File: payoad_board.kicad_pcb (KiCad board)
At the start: 2 copper layers, 48.8 x 58 mm, 3 parts, among them J1 NMHH-1_bus, U3 RP2040 MCU board, U4 RP2040 MCU board

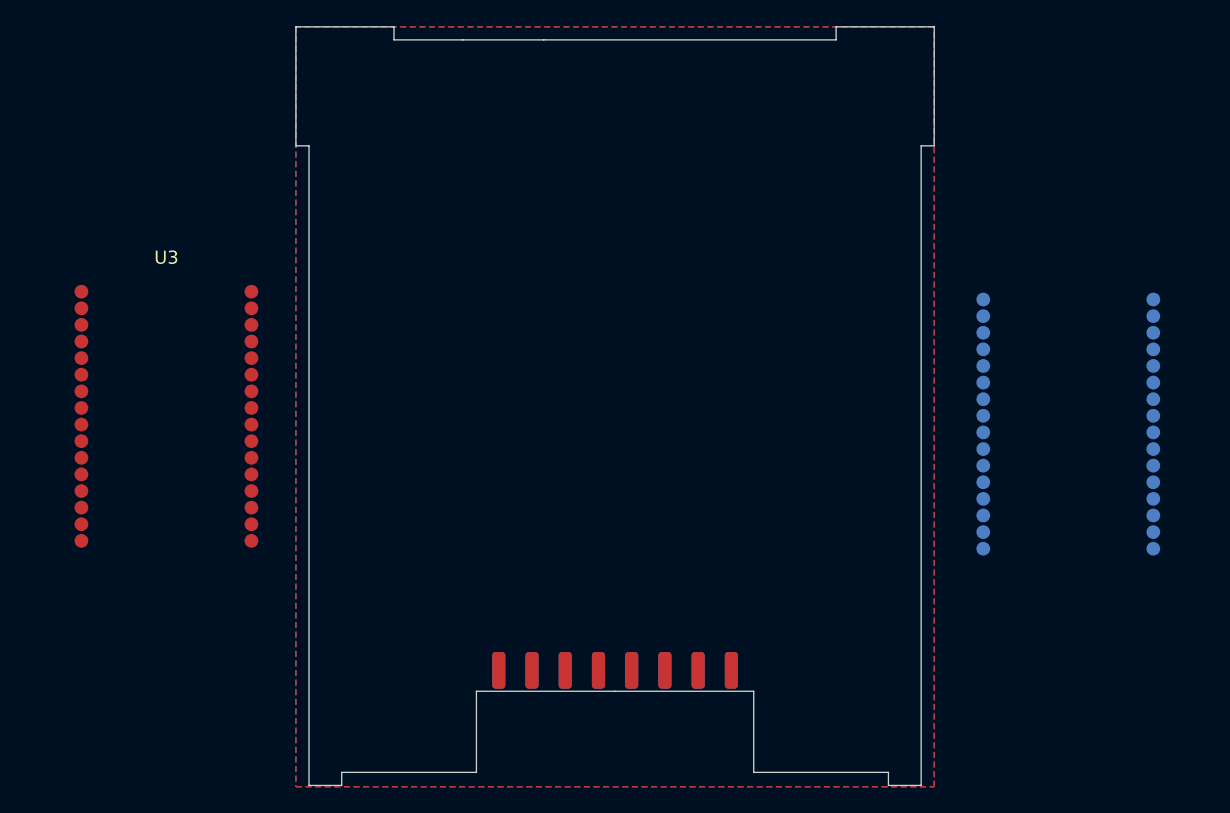
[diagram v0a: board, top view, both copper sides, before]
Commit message: Project libraries, PQ_bus connector symbol, CAN2 on the bus
- Add project-local symbol (pq.kicad_sym) and footprint library tables,
  both relative to ${KIPRJMOD}, so the project opens without extra setup
- New PQ_bus symbol: supply pins are power outputs, so ERC passes
  without PWR_FLAGs; replaces the generic 2x8 connector
- Bus connector footprint renamed to PQ_bus, 3D model assigned
- CAN2 routed to bus pins 6/8 (U2); CAN1 on pins 9/11 (U1)
- 1-Wire notes on the schematic, MCUs re-annotated to U1/U2
- README: PQ_bus pinout with DNC pins, library and file list

Co-Authored-By: Claude Opus 5.5 <noreply@anthropic.com>
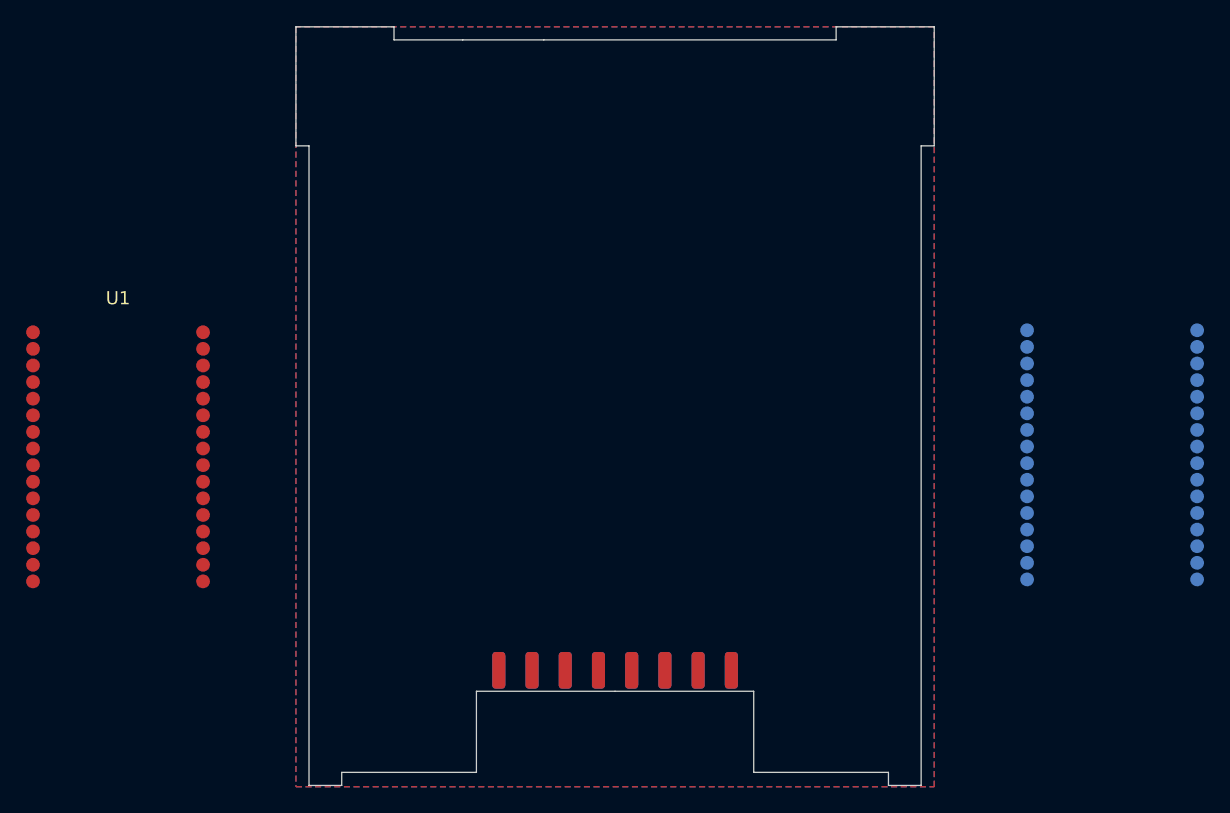
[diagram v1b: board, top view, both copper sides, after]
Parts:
- removed U3, U4: RP2040 MCU board, pq:MCU_board_127
- added U1: RP2040 MCU board, pq:MCU_board_127, F.Cu at (-38.0, -24.2)
- added U2: RP2040 MCU board, pq:MCU_board_127, B.Cu at (38.0, -24.2)
- J1: value NMHH-1_bus -> PQ_bus
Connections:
- J1 pad 6: CAN1_H -> CAN2_H
- J1 pad 8: CAN1_L -> CAN2_L

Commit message: Rename 1W/1-Wire signals to HDUART
1-Wire is a trademarked name, so the bus signals and MCU pin labels
are now called HDUART (HDUART_1, HDUART_2, GPIO05/HDUART1, ...).

Co-Authored-By: Claude Opus 5.5 <noreply@anthropic.com>
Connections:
- net 1W_1 renamed HDUART_1
- net 1W_2 renamed HDUART_2
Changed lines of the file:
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@@
 			(layers "B.Cu" "B.Mask" "B.Paste")
 			(roundrect_rratio 0.25)
-			(net "1W_2")
-			(pinfunction "1W_2_4")
+			(net "HDUART_2")
+			(pinfunction "HDUART_2_4")
 			(pintype "bidirectional")
 			(thermal_bridge_angle 45)
@@
 			(layers "F.Cu" "F.Mask" "F.Paste")
 			(roundrect_rratio 0.25)
-			(net "1W_1")
-			(pinfunction "1W_1_13")
+			(net "HDUART_1")
+			(pinfunction "HDUART_1_13")
 			(pintype "bidirectional")
 			(thermal_bridge_angle 45)
@@
 			)
 		)
-		(fp_text user "GPIO00_(1W2TX)"
+		(fp_text user "GPIO00_(HDUART2TX)"
 			(at -5.975 -8.18 0)
 			(unlocked yes)
@@
 			)
 		)
-		(fp_text user "GPIO01/1W2"
+		(fp_text user "GPIO01/HDUART2"
 			(at -5.975 -6.91 0)
 			(unlocked yes)
@@
 			)
 		)
-		(fp_text user "GPIO04_(1W1TX)"
+		(fp_text user "GPIO04_(HDUART1TX)"
 			(at -5.975 -3.1 0)
 			(unlocked yes)
@@
 			)
 		)
-		(fp_text user "GPIO05/1W1"
+		(fp_text user "GPIO05/HDUART1"
 			(at -5.975 -1.83 0)
 			(unlocked yes)
@@
 			(size 1.05 1.05)
 			(layers "F.Cu" "F.Mask" "F.Paste")
-			(net "unconnected-(U1-GPIO00_(1W2TX)-Pad2)")
-			(pinfunction "GPIO00_(1W2TX)_2")
+			(net "unconnected-(U1-GPIO00_(HDUART2TX)-Pad2)")
+			(pinfunction "GPIO00_(HDUART2TX)_2")
 			(pintype "bidirectional")
 		)
@@
 			(size 1.05 1.05)
 			(layers "F.Cu" "F.Mask" "F.Paste")
-			(net "unconnected-(U1-GPIO01{slash}1W2-Pad3)")
-			(pinfunction "GPIO01/1W2_3")
+			(net "unconnected-(U1-GPIO01{slash}HDUART2-Pad3)")
+			(pinfunction "GPIO01/HDUART2_3")
 			(pintype "bidirectional")
 		)
@@
 			(size 1.05 1.05)
 			(layers "F.Cu" "F.Mask" "F.Paste")
-			(net "unconnected-(U1-GPIO04_(1W1TX)-Pad6)")
-			(pinfunction "GPIO04_(1W1TX)_6")
+			(net "unconnected-(U1-GPIO04_(HDUART1TX)-Pad6)")
+			(pinfunction "GPIO04_(HDUART1TX)_6")
 			(pintype "bidirectional+no_connect")
 		)
@@
 			(size 1.05 1.05)
 			(layers "F.Cu" "F.Mask" "F.Paste")
-			(net "1W_1")
-			(pinfunction "GPIO05/1W1_7")
+			(net "HDUART_1")
+			(pinfunction "GPIO05/HDUART1_7")
 			(pintype "bidirectional")
 		)
@@
 			)
 		)
-		(fp_text user "GPIO05/1W1"
+		(fp_text user "GPIO05/HDUART1"
 			(at -5.975 1.83 180)
 			(unlocked yes)
@@
 			)
 		)
-		(fp_text user "GPIO04_(1W1TX)"
+		(fp_text user "GPIO04_(HDUART1TX)"
 			(at -5.975 3.1 180)
 			(unlocked yes)
@@
 			)
 		)
-		(fp_text user "GPIO01/1W2"
+		(fp_text user "GPIO01/HDUART2"
 			(at -5.975 6.91 180)
 			(unlocked yes)
@@
 			)
 		)
-		(fp_text user "GPIO00_(1W2TX)"
+		(fp_text user "GPIO00_(HDUART2TX)"
 			(at -5.975 8.18 180)
 			(unlocked yes)
@@
 			(size 1.05 1.05)
 			(layers "B.Cu" "B.Mask" "B.Paste")
-			(net "unconnected-(U2-GPIO00_(1W2TX)-Pad2)")
-			(pinfunction "GPIO00_(1W2TX)_2")
+			(net "unconnected-(U2-GPIO00_(HDUART2TX)-Pad2)")
+			(pinfunction "GPIO00_(HDUART2TX)_2")
 			(pintype "bidirectional+no_connect")
 		)
@@
 			(size 1.05 1.05)
 			(layers "B.Cu" "B.Mask" "B.Paste")
-			(net "1W_2")
-			(pinfunction "GPIO01/1W2_3")
+			(net "HDUART_2")
+			(pinfunction "GPIO01/HDUART2_3")
 			(pintype "bidirectional")
 		)
@@
 			(size 1.05 1.05)
 			(layers "B.Cu" "B.Mask" "B.Paste")
-			(net "unconnected-(U2-GPIO04_(1W1TX)-Pad6)")
-			(pinfunction "GPIO04_(1W1TX)_6")
+			(net "unconnected-(U2-GPIO04_(HDUART1TX)-Pad6)")
+			(pinfunction "GPIO04_(HDUART1TX)_6")
 			(pintype "bidirectional")
 		)
@@
 			(size 1.05 1.05)
 			(layers "B.Cu" "B.Mask" "B.Paste")
-			(net "unconnected-(U2-GPIO05{slash}1W1-Pad7)")
-			(pinfunction "GPIO05/1W1_7")
-			(pintype "bidirectional")
-		)
+			(net "unconnected-(U2-GPIO05{slash}HDUART1-Pad7)")
+			(pinfunction "GPIO05/HDUART1_7")
+			(pintype "bidirectional")
+		)
